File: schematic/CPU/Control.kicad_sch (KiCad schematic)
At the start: 21 parts, among them U106 74LS32, U38 74LS08, U59 74LS08, U78 74LS08, U81 74LS86, U82 74LS08, U83 74AS825, U84 74LS374, U85 28C256, U86 28C256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

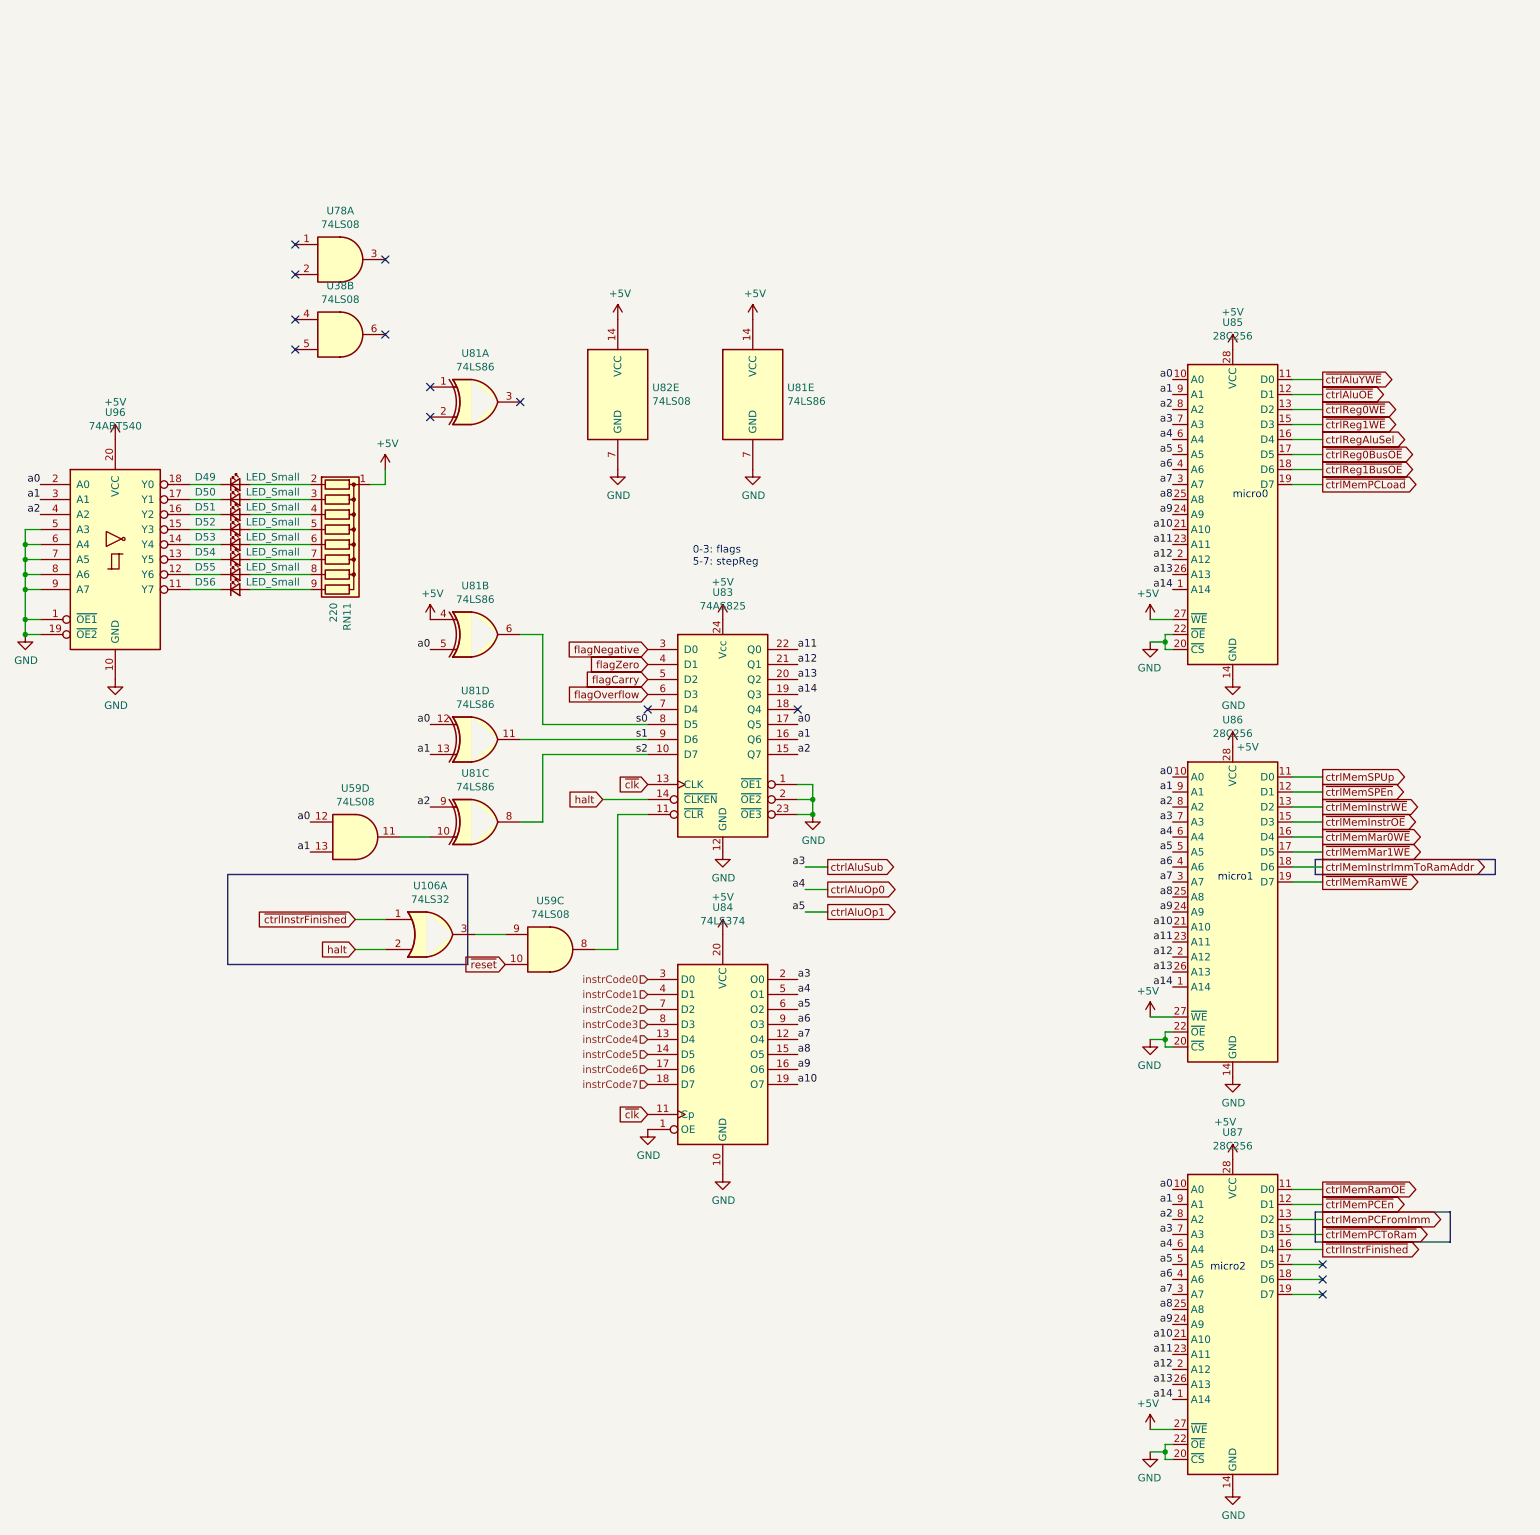
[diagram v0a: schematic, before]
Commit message: ttl fpga: factorization works in sim and fpga
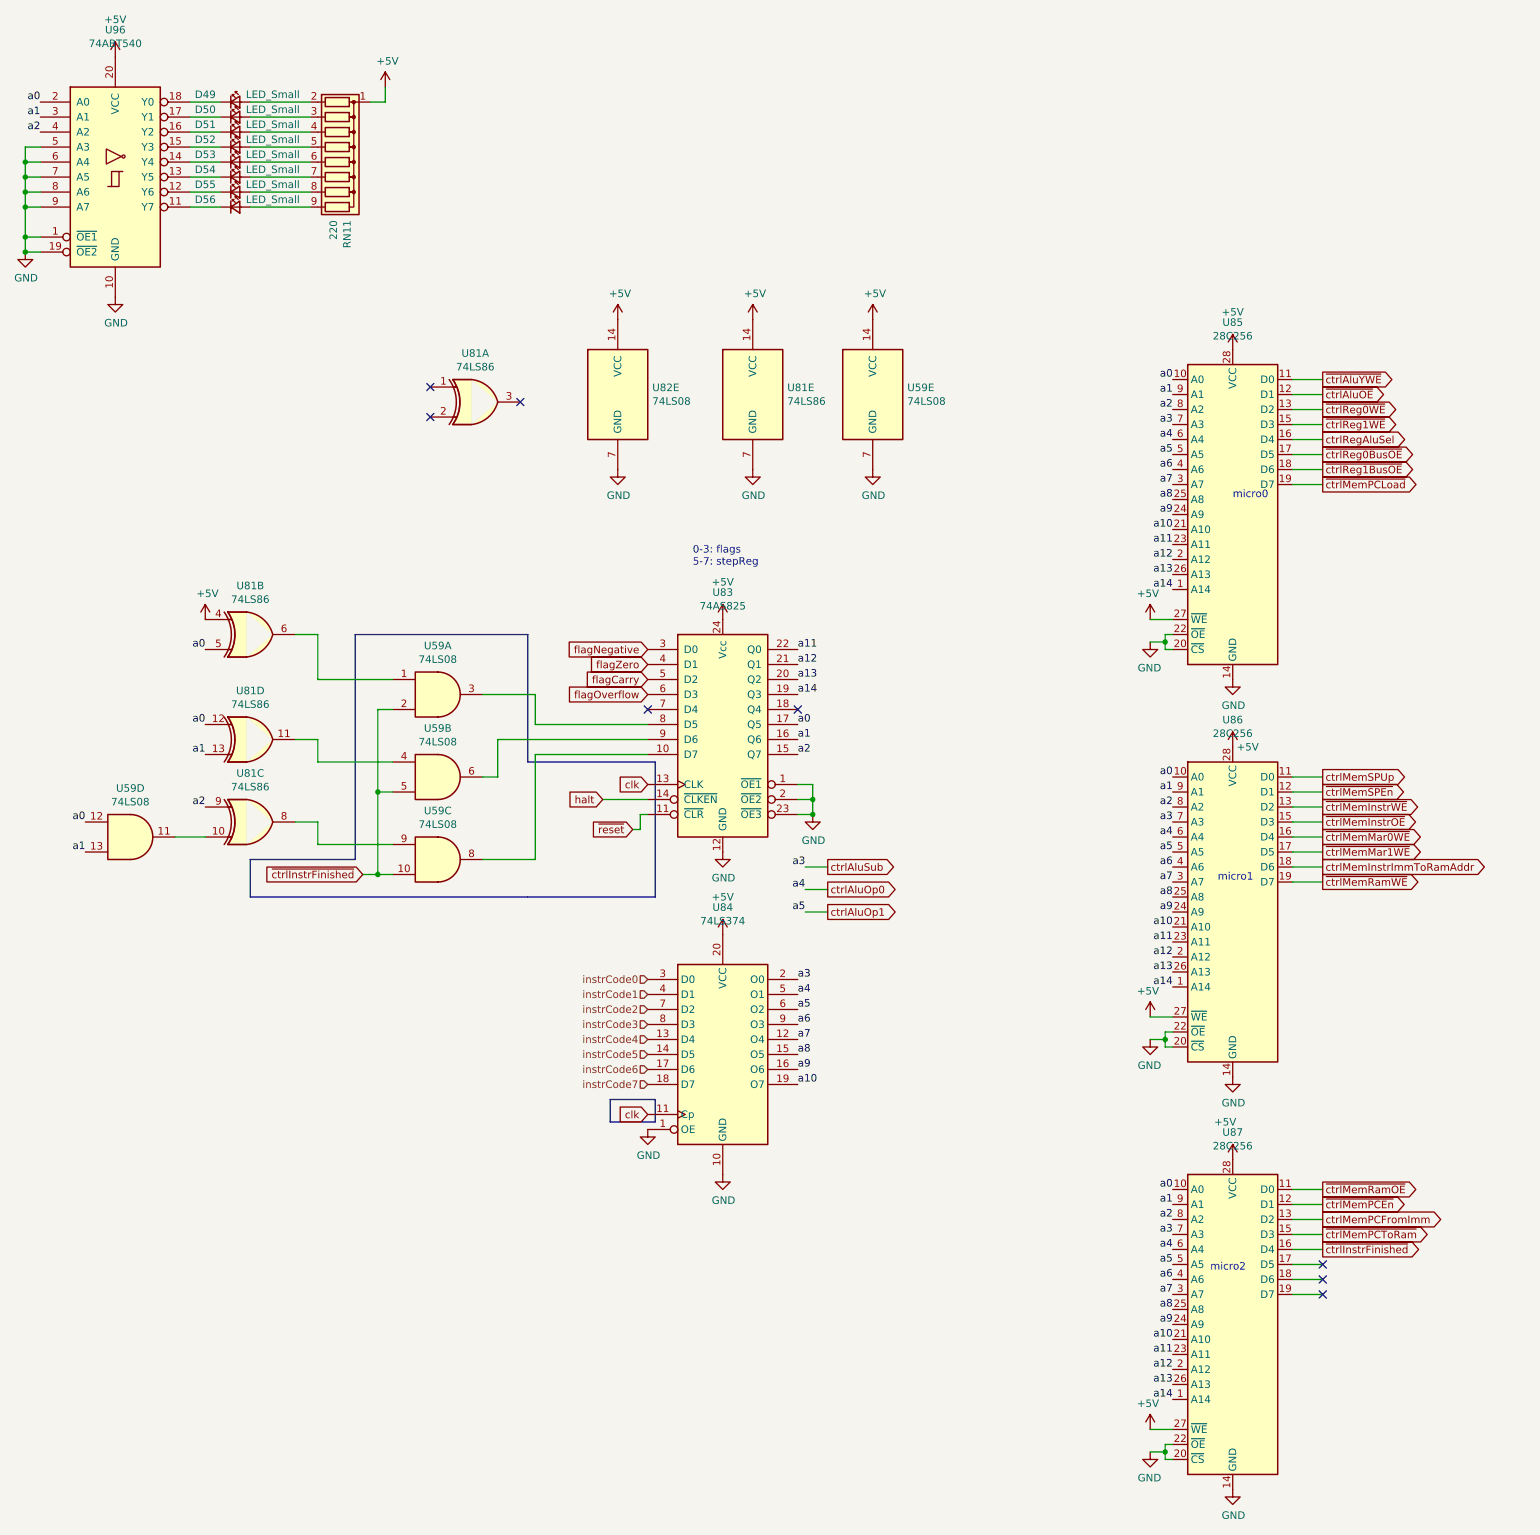
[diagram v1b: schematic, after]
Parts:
- removed U106: 74LS32, symbol 74xx:74LS32
- removed U38, U78: 74LS08, Package_DIP:DIP-14_W7.62mm, symbol 74xx:74LS08
- added unit 2 of U59
- added unit 5 of U59
- added unit 1 of U59
- U59: footprint Package_DIP:DIP-14_W7.62mm -> (none)
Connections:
- net +5V: now also U59.14 (VCC)
- net GND: now also U59.7 (GND)
- net ~{ctrlInstrFinished}: now also U59.10, U59.2, U59.5
- net ~{reset}: now also U83.11 (~{CLR}); no longer U59.10
- net at U59.8: now also U83.10 (D7); no longer U83.11 (~{CLR})
- net at U59.9: now also U81.8
- net s0: no longer names the net of U81.6
- net s0: now also U59.1; no longer U83.8 (D5)
- net s1: no longer names the net of U81.11
- net s1: now also U59.4; no longer U83.9 (D6)
- removed net s2: U81.8, U83.10 (D7)
- net ~{clk} renamed clk
- new net: U59.3, U83.8 (D5)
- new net: U59.6, U83.9 (D6)
- no-connect marks 14 -> 8
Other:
- moved on the sheet: D49, D50, D51, D52, D53, D54, D55, D56, RN11, U59D, U81B, U81C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
